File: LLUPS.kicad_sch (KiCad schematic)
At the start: 0 parts

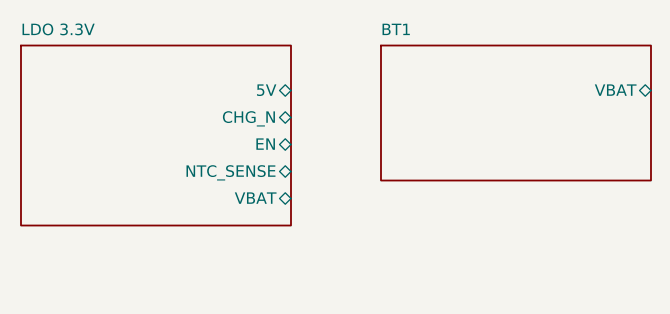
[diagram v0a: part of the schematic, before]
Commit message: chore: rename BT1 leaf sheet -> BATT to disambiguate from BT1 component
BT1 was both the schematic-sheet name for the battery subcircuit AND
the reference designator of the BT1 18650 cell that lives inside it.
Reading code/logs that say "BT1" was ambiguous: do you mean the leaf
or the part?

- BT1.kicad_sch -> BATT.kicad_sch (file rename, contents unchanged)
- LLUPS.kicad_sch hierarchical sheet entry: Sheetname "BT1" -> "BATT",
  Sheetfile "BT1.kicad_sch" -> "BATT.kicad_sch"

Component refs (BT1, BT2 the actual cell designators) and any code
referring to those component names are unchanged. LLUPS_autoplacer.json
ic_groups / group_labels / component_zones key on the BT1 component
reference, so they're unaffected. Stale .experiments/subcircuits/
artifact dir for the leaf was cleared so its metadata.json doesn't
keep advertising sheet_name="BT1".

Hierarchy parser confirmed: leaves now report as
  USB INPUT, CHARGER, BATT PROT, BOOST 5V, LDO 3.3V, BATT

Co-Authored-By: Claude Opus 4.7 (1M context) <noreply@anthropic.com>
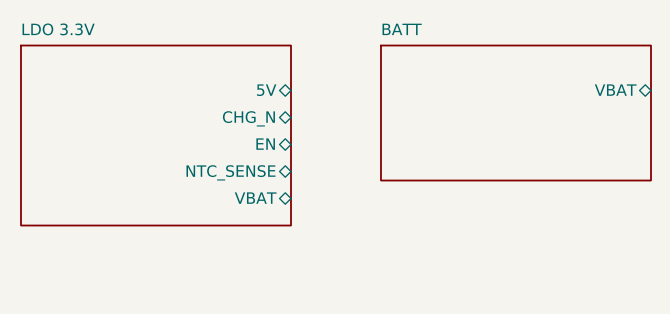
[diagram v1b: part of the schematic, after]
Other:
- sheet BT1 renamed BATT
- sheet BATT: file BT1.kicad_sch -> BATT.kicad_sch
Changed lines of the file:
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@@
 			(color 255 255 194 1)
 		)
-		(property "Sheetname" "BT1"
+		(property "Sheetname" "BATT"
 			(at 230 39 0)
 			(effects (font (size 1.27 1.27)) (justify left bottom))
 		)
-		(property "Sheetfile" "BT1.kicad_sch"
+		(property "Sheetfile" "BATT.kicad_sch"
 			(at 230 56 0)
 			(effects (font (size 1.27 1.27)) (justify left top) (hide yes))
